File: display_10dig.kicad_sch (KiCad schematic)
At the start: 35 parts, among them J1 2x09, J2 2x06, J3 02x03, Q1 MMBT3906, Q10 MMBT3906, Q2 MMBT3906, Q3 MMBT3906, Q4 MMBT3906, Q5 MMBT3906, Q6 MMBT3906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

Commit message: update to kicad 7.0
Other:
- company: (none) -> S59MZ
- title: (none) -> 10-Digit display with keyboard

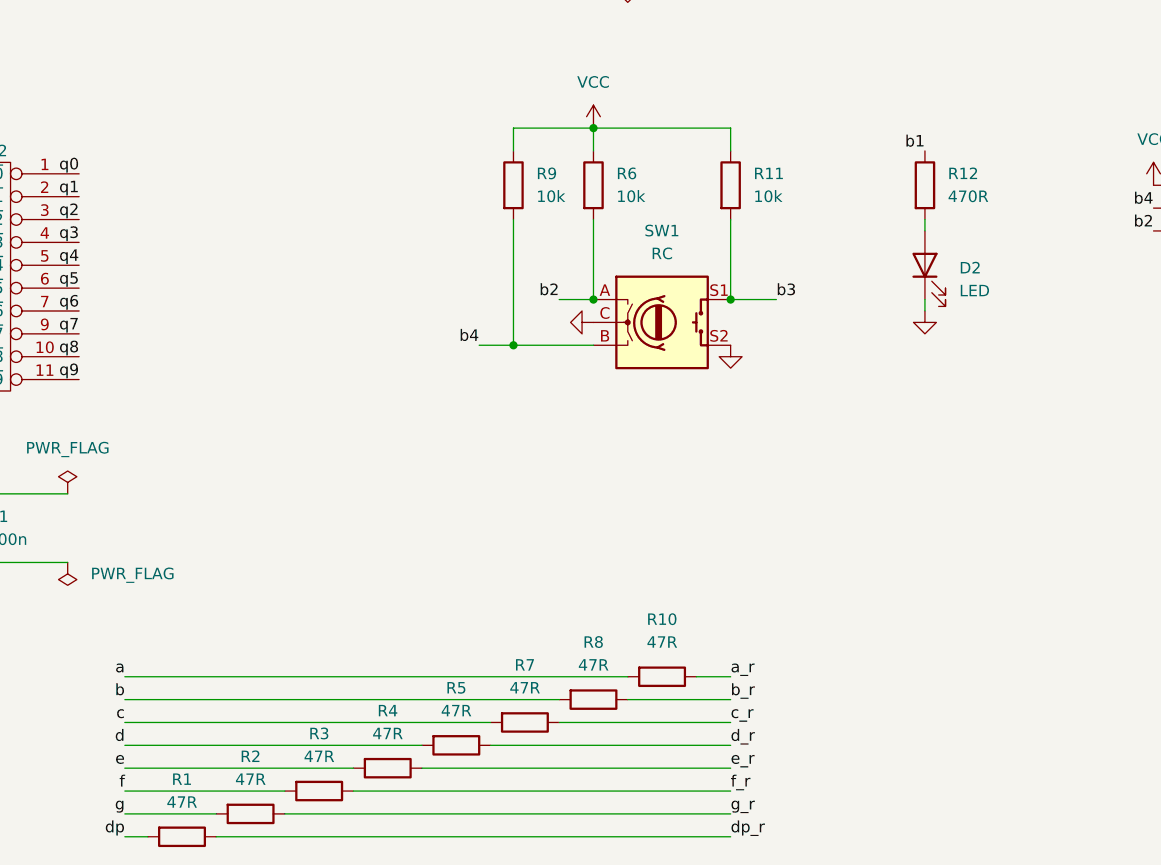
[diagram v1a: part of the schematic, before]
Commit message: updated resistoor values
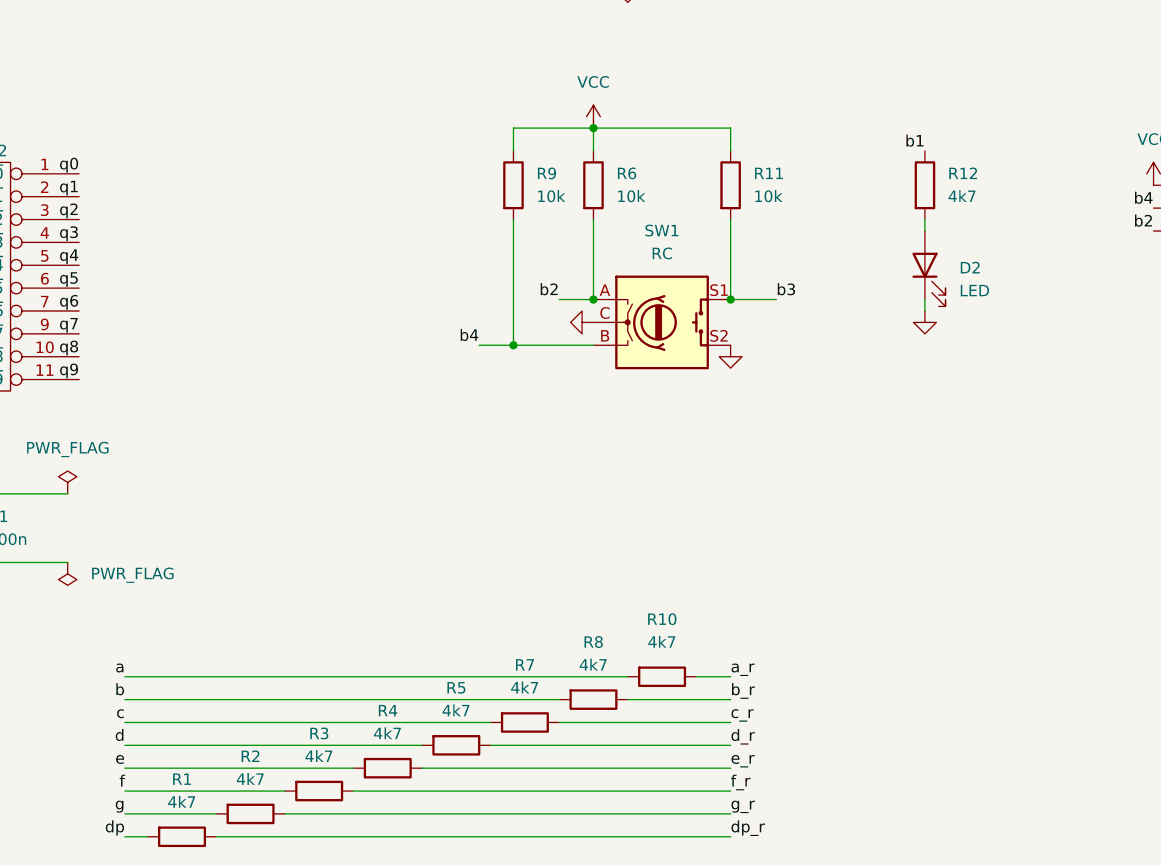
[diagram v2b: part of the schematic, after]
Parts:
- R1, R10, R2, R3, R4, R5, R7, R8: value 47R -> 4k7
- R12: value 470R -> 4k7
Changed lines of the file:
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@@
       (effects (font (size 1.27 1.27)))
     )
-    (property "Value" "47R" (at 163.83 172.72 90)
+    (property "Value" "4k7" (at 163.83 172.72 90)
       (effects (font (size 1.27 1.27)))
     )
@@
       (effects (font (size 1.27 1.27)))
     )
-    (property "Value" "47R" (at 148.59 177.8 90)
+    (property "Value" "4k7" (at 148.59 177.8 90)
       (effects (font (size 1.27 1.27)))
     )
@@
   (symbol (lib_id "Device:R") (at 193.04 121.92 0) (unit 1)
     (in_bom yes) (on_board yes) (dnp no) (fields_autoplaced)
-    (property "Reference" "R12" (at 195.58 120.6499 0)
-      (effects (font (size 1.27 1.27)) (justify left))
-    )
-    (property "Value" "470R" (at 195.58 123.1899 0)
+    (property "Reference" "R12" (at 195.58 120.65 0)
+      (effects (font (size 1.27 1.27)) (justify left))
+    )
+    (property "Value" "4k7" (at 195.58 123.19 0)
       (effects (font (size 1.27 1.27)) (justify left))
     )
@@
       (effects (font (size 1.27 1.27)))
     )
-    (property "Value" "47R" (at 140.97 180.34 90)
+    (property "Value" "4k7" (at 140.97 180.34 90)
       (effects (font (size 1.27 1.27)))
     )
@@
       (effects (font (size 1.27 1.27)))
     )
-    (property "Value" "47R" (at 110.49 190.5 90)
+    (property "Value" "4k7" (at 110.49 190.5 90)
       (effects (font (size 1.27 1.27)))
     )
@@
       (effects (font (size 1.27 1.27)))
     )
-    (property "Value" "47R" (at 133.35 182.88 90)
+    (property "Value" "4k7" (at 133.35 182.88 90)
       (effects (font (size 1.27 1.27)))
     )
@@
       (effects (font (size 1.27 1.27)))
     )
-    (property "Value" "47R" (at 125.73 185.42 90)
+    (property "Value" "4k7" (at 125.73 185.42 90)
       (effects (font (size 1.27 1.27)))
     )
@@
       (effects (font (size 1.27 1.27)))
     )
-    (property "Value" "47R" (at 118.11 187.96 90)
+    (property "Value" "4k7" (at 118.11 187.96 90)
       (effects (font (size 1.27 1.27)))
     )
@@
       (effects (font (size 1.27 1.27)))
     )
-    (property "Value" "47R" (at 156.21 175.26 90)
-      (effects (font (size 1.27 1.27)))
-    )
+    (property "Value" "4k7" (at 156.21 175.26 90)
+      (effects (font (size 1.27 1.27)))
+    )
